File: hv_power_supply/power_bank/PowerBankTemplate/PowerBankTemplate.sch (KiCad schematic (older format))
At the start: 0 parts

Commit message: Start layout for schematic
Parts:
- added C?: C_10uF, footprints:C_0805_OEM, symbol formula:C_10uF
- added C?: C_0.1uF, footprints:C_0805_OEM, symbol formula:C_0.1uF
- added C?: C_2.2uF, footprints:C_0805_OEM, symbol formula:C_2.2uF
- added C?: C_100uF, footprints:C_1812_OEM, symbol formula:C_100uF
- added D? (x2): LED_0805, footprints:LED_0805_OEM, symbol formula:LED_0805
- added L?: L_6.8uH, footprints:L_100uH_OEM, symbol formula:L_6.8uH
- added Q?: MMUN2133LT1G, SOT95P240X111-3N, symbol formula:MMUN2133LT1G
- added R?: R_100K, footprints:R_0805_OEM, symbol formula:R_100K
- added R? (x2): R_1.87M, footprints:R_0805_OEM, symbol formula:R_1.87M
- added R?: R_340K, footprints:R_0805_OEM, symbol formula:R_340K
- added R? (x2): R_200K, footprints:R_0805_OEM, symbol formula:R_200K
- added R? (x2): R_1K, footprints:R_0805_OEM, symbol formula:R_1K
- added U?: MCP73871T-2CCI_ML, footprints:MCP73871T, symbol formula:MCP73871T-2CCI_ML
- added U?: TPS61090RSAR, footprints:TPS61090RSAR, symbol formula:TPS61090RSAR
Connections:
- net labels added: +5V, +BATT, ENABLE, GND
- wire segments 0 -> 39

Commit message: First Pass new member schemati
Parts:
- removed R?: R_100K, footprints:R_0805_OEM, symbol formula:R_100K
- added C?: C_10nF, footprints:C_0805_OEM, symbol formula:C_10nF
- added C?: C_10uF, footprints:C_0805_OEM, symbol formula:C_10uF
- added D?: LED_0805_Amber, footprints:LED_0805_OEM, symbol formula:LED_0805_Amber
- added D?: LED_0805_Red, footprints:LED_0805_OEM, symbol formula:LED_0805_Red
- added R? (x2): R_100K, footprints:R_0805_OEM, symbol formula:R_100K
- added R?: R_270K, footprints:R_0805_OEM, symbol formula:R_270K
- added R? (x2): R_1K, footprints:R_0805_OEM, symbol formula:R_1K
- added R?: R_1.8K, footprints:R_0805_OEM, symbol formula:R_1.8K
- added TP?: TP, footprints:tp_1.6mm, symbol formula:TP
- added U?: USB_MicroB, Connectors_USB:USB_Micro-B_Molex-105017-0001, symbol formula:USB_MicroB
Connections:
- net labels added: 16KThermistor, VBUS, batteryconnection
- wire segments 39 -> 75
- no-connect marks 0 -> 5
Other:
- moved on the sheet: U?

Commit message: Minor changes for clarity
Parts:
- removed Q?: MMUN2133LT1G, SOT95P240X111-3N, symbol formula:MMUN2133LT1G
- added J?: USB_A, symbol Connector:USB_A
- added Q?: SSM3K333R, footprints:SOT-23F, symbol formula:SSM3K333R
- added R?: R_10K, footprints:R_0805_OEM, symbol formula:R_10K
- R?: symbol formula:R_1.8K -> PowerBankTemplate-rescue:R_1.8K-formula
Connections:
- wire segments 75 -> 76
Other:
- note added: "Charging LED"
- note added: "Input/Output"
- moved on the sheet: C?, D?, R?, TP?, U?

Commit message: Final Draft of power bank template schematic. Ready for review
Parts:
- removed R?: R_1.8K, footprints:R_0805_OEM, symbol PowerBankTemplate-rescue:R_1.8K-formula
- added C1: C_10uF, footprints:C_0805_OEM, symbol formula:C_10uF
- added F1: 1.5A_Fuse, footprints:Fuse_1206, symbol formula:1.5A_Fuse
- added J1, J2: CONN_01x02, Connector_PinHeader_2.54mm:PinHeader_1x02_P2.54mm_Vertical, symbol formula:CONN_01x02
- added R1: R_75k, footprints:R_0805_OEM, symbol formula:R_49.9K
- added R14: R_1K, footprints:R_0805_OEM, symbol formula:R_1K
- added R2, R4: R_49.9K, footprints:R_0805_OEM, symbol formula:R_49.9K
- added R3: R_43k, footprints:R_0805_OEM, symbol formula:R_49.9K
- gave numbers to parts that had none: 30
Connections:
- net labels added: Battery+
- net labels removed: batteryconnection
- wire segments 76 -> 101
- no-connect marks 5 -> 4
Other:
- note added: "+5V"
- note added: "+Batt"
- note added: "Battery"
- note added: "Battery + Load Manager"
- note added: "Battery+"
- note added: "Boost Converter"
- note added: "Input USB\n(to charge bat)"
- note added: "Low Battery Indicator"
- note added: "MCP"
- note added: "Micro USB"
- note added: "Output USB\n (to charge phone)"
- note added: "Power Bank Project"
- note added: "Power Flow"
- note added: "Power LED"
- note added: "TI-Boost"
- note added: "Thermistor"
- note added: "USB-A"
- note added: "Vbus"
- note removed: "Charging LED"
- note removed: "Input/Output"
- moved on the sheet: C2, C3, C4, C5, C6, C7, D2, D3, D4, J3, L1, Q1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

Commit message: Minor Updates to HVPS New Member Schematic
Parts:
- removed D1: LED_0805_Red, footprints:LED_0805_OEM, symbol formula:LED_0805_Red
- added D?: LED_0805, footprints:LED_0805_OEM, symbol formula:LED_0805
- added TP2, TP3, TP4, TP?: TP, footprints:tp_1.6mm, symbol formula:TP
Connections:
- net labels removed: ENABLE
- wire segments 101 -> 107
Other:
- note added: "Charging"
- note added: "Done Charging"
- note added: "resistor values are specific to iOS -\n to charge other devices, \nchange values accordingly"
- moved on the sheet: D2
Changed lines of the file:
@@
 encoding utf-8
 Sheet 1 1
-Title "New Member Project Template"
-Date ""
-Rev ""
+Title "Power Bank Project"
+Date "2020-10-10"
+Rev "1"
 Comp "Olin Electric Motorsports"
-Comment1 "insert_name"
+Comment1 ""
 Comment2 ""
 Comment3 ""
@@
 	1    0    0    -1
 $EndComp
-Text Label 6600 1750 2    50   ~ 0
-ENABLE
 $Comp
 L power:GND #PWR014
@@
 	5650 1650 5950 1650
 Wire Wire Line
-	5300 1350 6300 1350
+	5300 1350 5600 1350
 $Comp
 L formula:R_1.87M R5
 U 1 1 5F7A4733
 P 5950 1800
-F 0 "R5" H 6000 1700 50  0000 L CNN
+F 0 "R5" H 5950 1650 50  0000 L CNN
 F 1 "R_1.87M" V 5850 1600 50  0000 L CNN
 F 2 "footprints:R_0805_OEM" H 5880 1800 50  0001 C CNN
@@
 U 1 1 5F7B6B11
 P 9100 1550
-F 0 "C7" H 9150 1450 50  0000 L CNN
+F 0 "C7" H 9050 1800 50  0000 L CNN
 F 1 "C_100uF" V 8950 1350 50  0000 L CNN
 F 2 "footprints:C_1812_OEM" H 9100 2300 50  0001 C CNN
@@
 U 1 1 5F7B7F51
 P 8500 1900
-F 0 "R12" H 8570 1946 50  0000 L CNN
+F 0 "R12" H 8550 1750 50  0000 L CNN
 F 1 "R_200K" V 8400 1750 50  0000 L CNN
 F 2 "footprints:R_0805_OEM" H 8430 1900 50  0001 C CNN
@@
 	8100 1900 8300 1900
 Wire Wire Line
-	8100 2100 8500 2100
+	8100 2100 8200 2100
 Wire Wire Line
 	8500 2050 8500 2100
@@
 Connection ~ 9100 1400
 Wire Wire Line
-	2200 5150 2750 5150
+	2200 5150 2450 5150
 Wire Wire Line
 	2750 5150 2750 4850
@@
 U 1 1 5F93A07E
 P 2350 2000
-F 0 "C1" H 2465 2096 50  0000 L CNN
-F 1 "C_10uF" H 2465 2005 50  0000 L CNN
+F 0 "C1" H 2400 2150 50  0000 L CNN
+F 1 "C_10uF" H 2350 1950 50  0000 L CNN
 F 2 "footprints:C_0805_OEM" H 2388 2600 50  0001 C CNN
 F 3 "http://www.samsungsem.com/kr/support/product-search/mlcc/__icsFiles/afieldfile/2018/06/20/CL21A106KPFNNNE.pdf" H 2375 2850 50  0001 C CNN
@@
 Power LED
 $Bitmap
-Pos 7850 4750
+Pos 7800 4850
 Scale 1.000000
 Data
@@
 	3800 4550 3800 4450
 Wire Wire Line
-	4350 4550 3800 4550
+	4350 4550 4000 4550
 Wire Wire Line
 	4350 4500 4350 4550
@@
 	6850 3800 7050 3800
 $Comp
-L formula:LED_0805_Red D1
-U 1 1 5F7CFFA7
+L formula:LED_0805_Amber D2
+U 1 1 5F7CF104
 P 6400 3800
-F 0 "D1" H 6400 3950 50  0000 R CNN
-F 1 "LED_0805_Red" H 6450 3850 50  0000 R CNN
+F 0 "D2" H 6550 3750 50  0000 R CNN
+F 1 "LED_0805_Amber" H 6600 3900 50  0000 R CNN
 F 2 "footprints:LED_0805_OEM" H 6300 3800 50  0001 C CNN
-F 3 "http://www.osram-os.com/Graphics/XPic8/00078869_0.pdf" H 6400 3900 50  0001 C CNN
+F 3 "https://media.digikey.com/pdf/Data%20Sheets/Chicago%20Miniature%20Lamps%20PDFs/CMDA5_Series_Rev_Aug_2014.pdf" H 6400 3900 50  0001 C CNN
 F 4 "DK" H 6400 3800 60  0001 C CNN "MFN"
-F 5 "475-1415-1-ND" H 6400 3800 60  0001 C CNN "MPN"
-F 6 "https://www.digikey.com/product-detail/en/osram-opto-semiconductors-inc/LH-R974-LP-1/475-1415-1-ND/1802604" H 6800 4300 60  0001 C CNN "PurchasingLink"
+F 5 "L71517CT-ND" H 6400 3800 60  0001 C CNN "MPN"
+F 6 "https://www.digikey.com/product-detail/en/visual-communications-company-vcc/CMDA5DY7D1S/L71517CT-ND/614867" H 6800 4300 60  0001 C CNN "PurchasingLink"
 	1    6400 3800
 	1    0    0    -1
 $EndComp
 $Comp
-L formula:LED_0805_Amber D2
-U 1 1 5F7CF104
-P 7150 3900
-F 0 "D2" H 7150 3800 50  0000 R CNN
-F 1 "LED_0805_Amber" H 6950 3850 50  0000 R CNN
-F 2 "footprints:LED_0805_OEM" H 7050 3900 50  0001 C CNN
-F 3 "https://media.digikey.com/pdf/Data%20Sheets/Chicago%20Miniature%20Lamps%20PDFs/CMDA5_Series_Rev_Aug_2014.pdf" H 7150 4000 50  0001 C CNN
-F 4 "DK" H 7150 3900 60  0001 C CNN "MFN"
-F 5 "L71517CT-ND" H 7150 3900 60  0001 C CNN "MPN"
-F 6 "https://www.digikey.com/product-detail/en/visual-communications-company-vcc/CMDA5DY7D1S/L71517CT-ND/614867" H 7550 4400 60  0001 C CNN "PurchasingLink"
-	1    7150 3900
-	1    0    0    -1
-$EndComp
-$Comp
 L formula:R_1K R17
 U 1 1 5F7CE5B8
@@
 Text Notes 6250 6050 0    157  Italic 0
 Power Bank Project
+$Comp
+L formula:TP TP4
+U 1 1 5F89A753
+P 6400 1750
+F 0 "TP4" V 6615 1642 50  0000 C CNN
+F 1 "TP" V 6524 1642 50  0000 C CNN
+F 2 "footprints:tp_1.6mm" H 6300 1650 50  0001 C CNN
+F 3 "http://www.keyelco.com/product-pdf.cfm?p=1314" H 6400 1750 50  0001 C CNN
+F 4 "DK" H 6500 1850 50  0001 C CNN "MFN"
+F 5 "36-5006-ND" H 6600 1950 50  0001 C CNN "MPN"
+F 6 "https://www.digikey.com/product-detail/en/keystone-electronics/5006/36-5006-ND/255330" H 6700 2050 50  0001 C CNN "PurchasingLink"
+	1    6400 1750
+	0    -1   -1   0
+$EndComp
+Connection ~ 6600 1750
+$Comp
+L formula:TP TP2
+U 1 1 5F8A8B5D
+P 2450 4950
+F 0 "TP2" H 2528 4888 50  0000 L CNN
+F 1 "TP" H 2528 4797 50  0000 L CNN
+F 2 "footprints:tp_1.6mm" H 2350 4850 50  0001 C CNN
+F 3 "http://www.keyelco.com/product-pdf.cfm?p=1314" H 2450 4950 50  0001 C CNN
+F 4 "DK" H 2550 5050 50  0001 C CNN "MFN"
+F 5 "36-5006-ND" H 2650 5150 50  0001 C CNN "MPN"
+F 6 "https://www.digikey.com/product-detail/en/keystone-electronics/5006/36-5006-ND/255330" H 2750 5250 50  0001 C CNN "PurchasingLink"
+	1    2450 4950
+	1    0    0    -1
+$EndComp
+Connection ~ 2450 5150
+Wire Wire Line
+	2450 5150 2750 5150
+$Comp
+L formula:TP TP3
+U 1 1 5F8BA2B0
+P 5600 1150
+F 0 "TP3" H 5678 1088 50  0000 L CNN
+F 1 "TP" H 5678 997 50  0000 L CNN
+F 2 "footprints:tp_1.6mm" H 5500 1050 50  0001 C CNN
+F 3 "http://www.keyelco.com/product-pdf.cfm?p=1314" H 5600 1150 50  0001 C CNN
+F 4 "DK" H 5700 1250 50  0001 C CNN "MFN"
+F 5 "36-5006-ND" H 5800 1350 50  0001 C CNN "MPN"
+F 6 "https://www.digikey.com/product-detail/en/keystone-electronics/5006/36-5006-ND/255330" H 5900 1450 50  0001 C CNN "PurchasingLink"
+	1    5600 1150
+	1    0    0    -1
+$EndComp
+Connection ~ 5600 1350
+Wire Wire Line
+	5600 1350 6300 1350
+Wire Wire Line
+	8100 1600 8200 1600
+Wire Wire Line
+	8200 1600 8200 2100
+Connection ~ 8200 2100
+Wire Wire Line
+	8200 2100 8500 2100
+$Comp
+L formula:TP TP?
+U 1 1 5F8580BF
+P 4000 4350
+F 0 "TP?" H 4078 4288 50  0000 L CNN
+F 1 "TP" H 4078 4197 50  0000 L CNN
+F 2 "footprints:tp_1.6mm" H 3900 4250 50  0001 C CNN
+F 3 "http://www.keyelco.com/product-pdf.cfm?p=1314" H 4000 4350 50  0001 C CNN
+F 4 "DK" H 4100 4450 50  0001 C CNN "MFN"
+F 5 "36-5006-ND" H 4200 4550 50  0001 C CNN "MPN"
+F 6 "https://www.digikey.com/product-detail/en/keystone-electronics/5006/36-5006-ND/255330" H 4300 4650 50  0001 C CNN "PurchasingLink"
+	1    4000 4350
+	1    0    0    -1
+$EndComp
+Connection ~ 4000 4550
+Wire Wire Line
+	4000 4550 3800 4550
+Text Notes 6100 3650 0    50   ~ 0
+Charging
+$Comp
+L formula:LED_0805 D?
+U 1 1 5F862D12
+P 7150 3900
+F 0 "D?" H 6900 3850 50  0000 C CNN
+F 1 "LED_0805" H 7100 3750 50  0000 C CNN
+F 2 "footprints:LED_0805_OEM" H 7050 3900 50  0001 C CNN
+F 3 "http://www.osram-os.com/Graphics/XPic9/00078860_0.pdf" H 7150 4000 50  0001 C CNN
+F 4 "DK" H 7150 3900 60  0001 C CNN "MFN"
+F 5 "475-1410-1-ND" H 7150 3900 60  0001 C CNN "MPN"
+F 6 "https://www.digikey.com/products/en?keywords=475-1410-1-ND" H 7550 4400 60  0001 C CNN "PurchasingLink"
+	1    7150 3900
+	1    0    0    -1
+$EndComp
+Text Notes 6850 4150 0    50   ~ 0
+Done Charging
+Text Notes 3300 1750 0    31   ~ 0
+resistor values are specific to iOS -\n to charge other devices, \nchange values accordingly
 $EndSCHEMATC

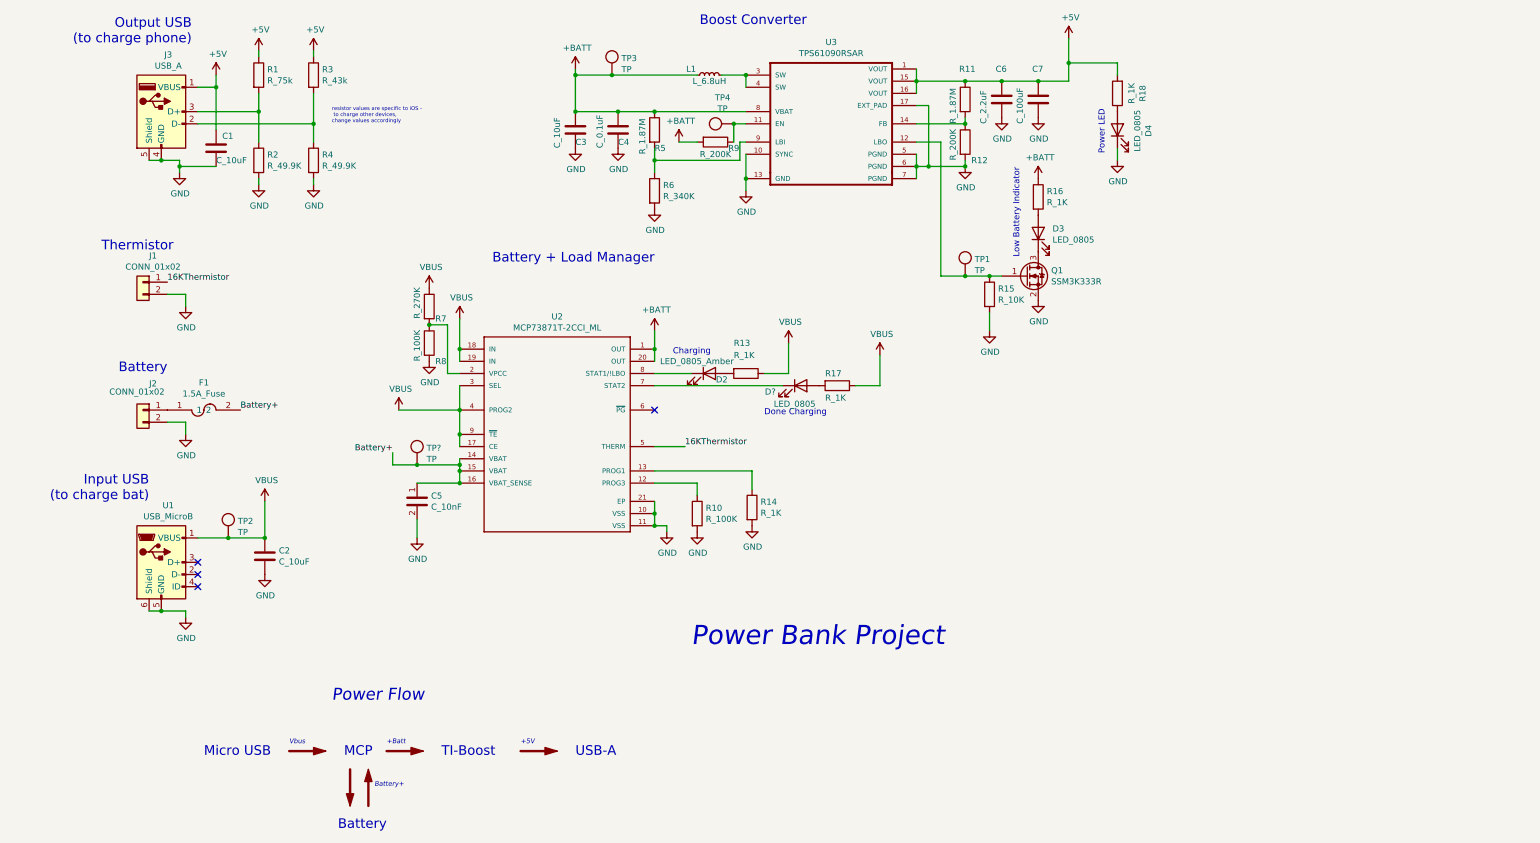
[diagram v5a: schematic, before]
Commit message: Update power symbol on new member sch
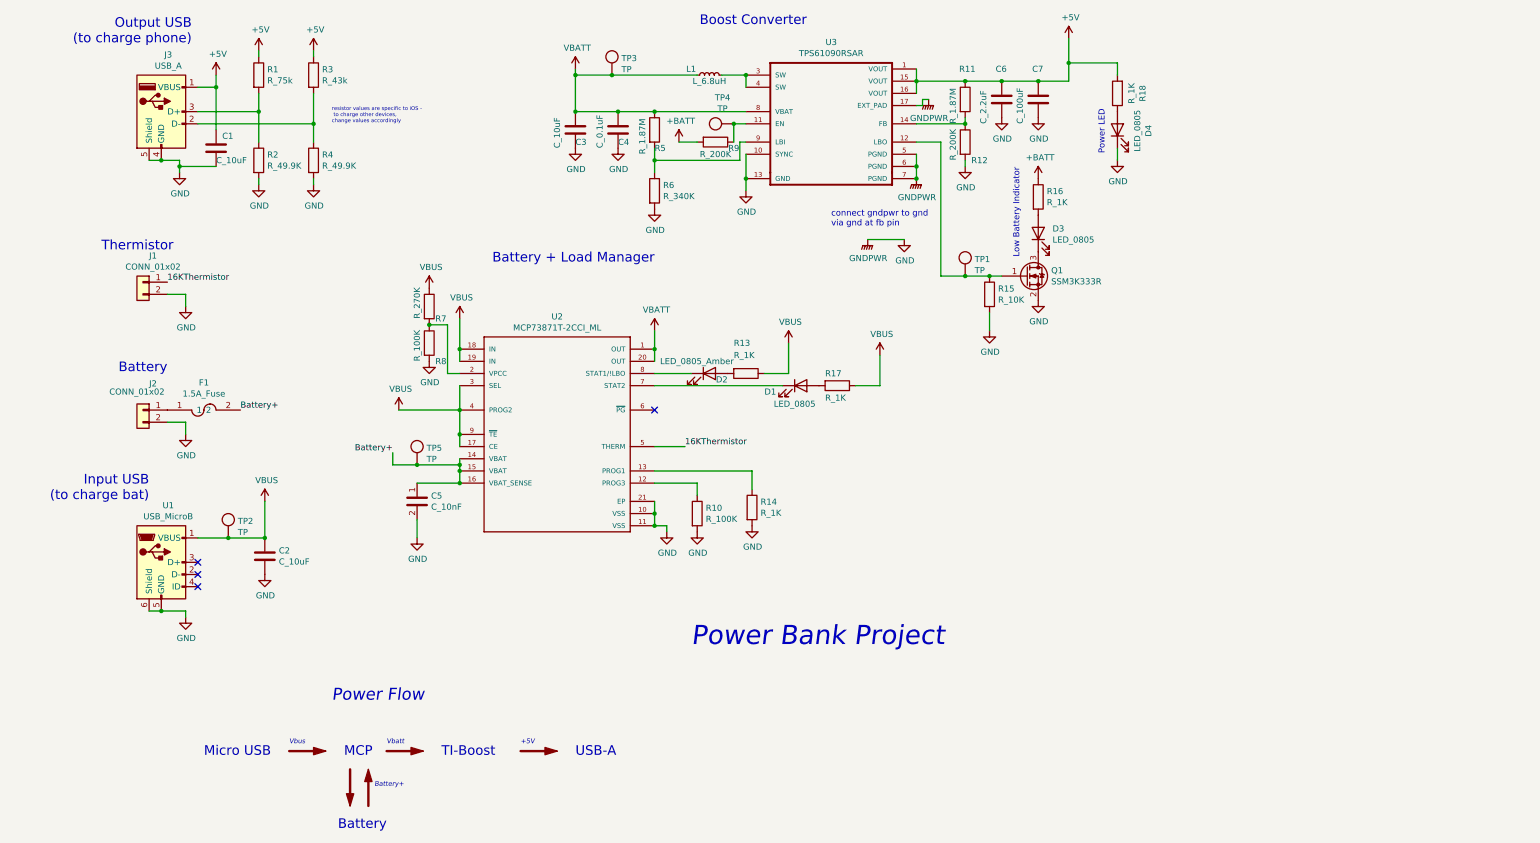
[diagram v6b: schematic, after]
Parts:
- gave numbers to parts that had none: 2
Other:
- note added: "Vbatt"
- note added: "connect gndpwr to gnd\nvia gnd at fb pin\n"
- note removed: "+Batt"
- note removed: "Charging"
- note removed: "Done Charging"
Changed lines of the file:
@@
-	1    0    0    -1
-$EndComp
-$Comp
-L power:+BATT #PWR012
-U 1 1 5F7AC017
-P 5300 1300
-F 0 "#PWR012" H 5300 1150 50  0001 C CNN
-F 1 "+BATT" H 5315 1473 50  0000 C CNN
-F 2 "" H 5300 1300 50  0001 C CNN
-F 3 "" H 5300 1300 50  0001 C CNN
-	1    5300 1300
 	1    0    0    -1
 $EndComp
@@
 	8100 1900 8300 1900
 Wire Wire Line
-	8100 2100 8200 2100
-Wire Wire Line
 	8500 2050 8500 2100
-Connection ~ 8500 2100
 $Comp
 L power:+BATT #PWR032
@@
 Vbus
 Text Notes 3750 6850 0    39   Italic 0
-+Batt
+Vbatt
 Text Notes 3650 7200 0    39   Italic 0
 Battery+
@@
 	1    0    0    -1
 $EndComp
-$Comp
-L power:+BATT #PWR023
-U 1 1 5F7C7758
-P 5950 3450
-F 0 "#PWR023" H 5950 3300 50  0001 C CNN
-F 1 "+BATT" H 5965 3623 50  0000 C CNN
-F 2 "" H 5950 3450 50  0001 C CNN
-F 3 "" H 5950 3450 50  0001 C CNN
-	1    5950 3450
-	1    0    0    -1
-$EndComp
 Connection ~ 5950 3600
 Wire Wire Line
@@
 Wire Wire Line
 	5600 1350 6300 1350
-Wire Wire Line
-	8100 1600 8200 1600
-Wire Wire Line
-	8200 1600 8200 2100
-Connection ~ 8200 2100
-Wire Wire Line
-	8200 2100 8500 2100
-$Comp
-L formula:TP TP?
+$Comp
+L formula:TP TP5
 U 1 1 5F8580BF
 P 4000 4350
-F 0 "TP?" H 4078 4288 50  0000 L CNN
+F 0 "TP5" H 4078 4288 50  0000 L CNN
 F 1 "TP" H 4078 4197 50  0000 L CNN
 F 2 "footprints:tp_1.6mm" H 3900 4250 50  0001 C CNN
@@
 Wire Wire Line
 	4000 4550 3800 4550
-Text Notes 6100 3650 0    50   ~ 0
-Charging
-$Comp
-L formula:LED_0805 D?
+$Comp
+L formula:LED_0805 D1
 U 1 1 5F862D12
 P 7150 3900
-F 0 "D?" H 6900 3850 50  0000 C CNN
+F 0 "D1" H 6900 3850 50  0000 C CNN
 F 1 "LED_0805" H 7100 3750 50  0000 C CNN
 F 2 "footprints:LED_0805_OEM" H 7050 3900 50  0001 C CNN
@@
 	1    0    0    -1
 $EndComp
-Text Notes 6850 4150 0    50   ~ 0
-Done Charging
 Text Notes 3300 1750 0    31   ~ 0
 resistor values are specific to iOS -\n to charge other devices, \nchange values accordingly
+$Comp
+L formula:GNDPWR #PWR037
+U 1 1 5F873BE1
+P 8100 2200
+F 0 "#PWR037" H 8100 2000 50  0001 C CNN
+F 1 "GNDPWR" H 8104 2046 50  0000 C CNN
+F 2 "" H 8100 2150 50  0001 C CNN
+F 3 "" H 8100 2150 50  0001 C CNN
+	1    8100 2200
+	1    0    0    -1
+$EndComp
+Connection ~ 8100 2200
+Text Notes 7400 2600 0    50   ~ 0
+connect gndpwr to gnd\nvia gnd at fb pin\n
+$Comp
+L formula:VBATT #PWR023
+U 1 1 5F89B24E
+P 5950 3450
+F 0 "#PWR023" H 5950 3300 50  0001 C CNN
+F 1 "VBATT" H 5965 3623 50  0000 C CNN
+F 2 "" H 5950 3450 50  0001 C CNN
+F 3 "" H 5950 3450 50  0001 C CNN
+	1    5950 3450
+	1    0    0    -1
+$EndComp
+$Comp
+L formula:VBATT #PWR012
+U 1 1 5F8A3001
+P 5300 1300
+F 0 "#PWR012" H 5300 1150 50  0001 C CNN
+F 1 "VBATT" H 5315 1473 50  0000 C CNN
+F 2 "" H 5300 1300 50  0001 C CNN
+F 3 "" H 5300 1300 50  0001 C CNN
+	1    5300 1300
+	1    0    0    -1
+$EndComp
+$Comp
+L formula:GNDPWR #PWR0101
+U 1 1 5F8CC586
+P 8200 1550
+F 0 "#PWR0101" H 8200 1350 50  0001 C CNN
+F 1 "GNDPWR" H 8204 1396 50  0000 C CNN
+F 2 "" H 8200 1500 50  0001 C CNN
+F 3 "" H 8200 1500 50  0001 C CNN
+	1    8200 1550
+	1    0    0    -1
+$EndComp
+Wire Wire Line
+	8100 1600 8150 1600
+Wire Wire Line
+	8150 1600 8150 1550
+Wire Wire Line
+	8150 1550 8200 1550
+$Comp
+L formula:GNDPWR #PWR?
+U 1 1 5F8EA6AD
+P 7700 2700
+F 0 "#PWR?" H 7700 2500 50  0001 C CNN
+F 1 "GNDPWR" H 7704 2546 50  0000 C CNN
+F 2 "" H 7700 2650 50  0001 C CNN
+F 3 "" H 7700 2650 50  0001 C CNN
+	1    7700 2700
+	1    0    0    -1
+$EndComp
+$Comp
+L power:GND #PWR?
+U 1 1 5F8EAEBF
+P 8000 2700
+F 0 "#PWR?" H 8000 2450 50  0001 C CNN
+F 1 "GND" H 8005 2527 50  0000 C CNN
+F 2 "" H 8000 2700 50  0001 C CNN
+F 3 "" H 8000 2700 50  0001 C CNN
+	1    8000 2700
+	1    0    0    -1
+$EndComp
+Wire Wire Line
+	7700 2700 8000 2700
 $EndSCHEMATC
